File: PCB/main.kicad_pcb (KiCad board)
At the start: 2 copper layers, 112.9 x 63.7 mm, 126 parts, among them K1 HK19F-DCxxV-SHC, Q1 BC807, Q10 BC817, Q11 BC817, Q12 TPCA8120,L1Q, Q13 BC817, Q14 BC817, Q15 BC817, Q16 TPCA8120,L1Q, Q17 BC817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

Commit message: FET's Gate to NPN's collector resistor removed
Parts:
- removed RA15, RA16, RA17, RA18, RA19: 33K, Resistor_SMD:R_1206_3216Metric
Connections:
- Q12 pad 4: Net-(Q12-G) -> Net-(Q11-C)
- Q16 pad 4: Net-(Q16-G) -> Net-(Q13-C)
- Q7 pad 4: Net-(Q7-G) -> Net-(Q10-C)
- Q8 pad 3: Net-(Q8-C) -> Net-(Q5-G)
- Q9 pad 3: Net-(Q9-C) -> Net-(Q6-G)
- RA11 pad 2: Net-(Q7-G) -> Net-(Q10-C)
- RA12 pad 2: Net-(Q12-G) -> Net-(Q11-C)
- RA13 pad 2: Net-(Q16-G) -> Net-(Q13-C)
- RA3 pad 1: Net-(Q9-C) -> Net-(Q6-G)
- RA4 pad 1: Net-(Q8-C) -> Net-(Q5-G)
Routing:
- net Net-(Q11-C): track 30.2 -> 112.8 mm, vias 2 -> 4
- net Net-(Q12-G): track 81.4 -> 0.00 mm, vias 3 -> 0
- net Net-(Q13-C): track 61.2 -> 141.0 mm, vias 3 -> 8
- net Net-(Q16-G): track 76.9 -> 0.00 mm, vias 5 -> 0
- net Net-(Q5-G): track 64.2 -> 107.2 mm, vias 1 -> 3
- net Net-(Q8-C): track 40.1 -> 0.00 mm, vias 2 -> 0
- net Net-(Q10-C): track 79.0 -> 117.6 mm, vias 3 -> 4
- net Net-(Q7-G): track 35.6 -> 0.00 mm, vias 1 -> 0
- net +12V: track 268.3 -> 240.2 mm
- net Net-(Q6-G): track 129.5 -> 147.8 mm, vias 5 -> 6
- net Net-(Q9-C): track 18.3 -> 0.00 mm, vias 1 -> 0
- net ci_engineOFF: track 129.3 -> 126.4 mm
- net GND: track 501.9 -> 500.7 mm

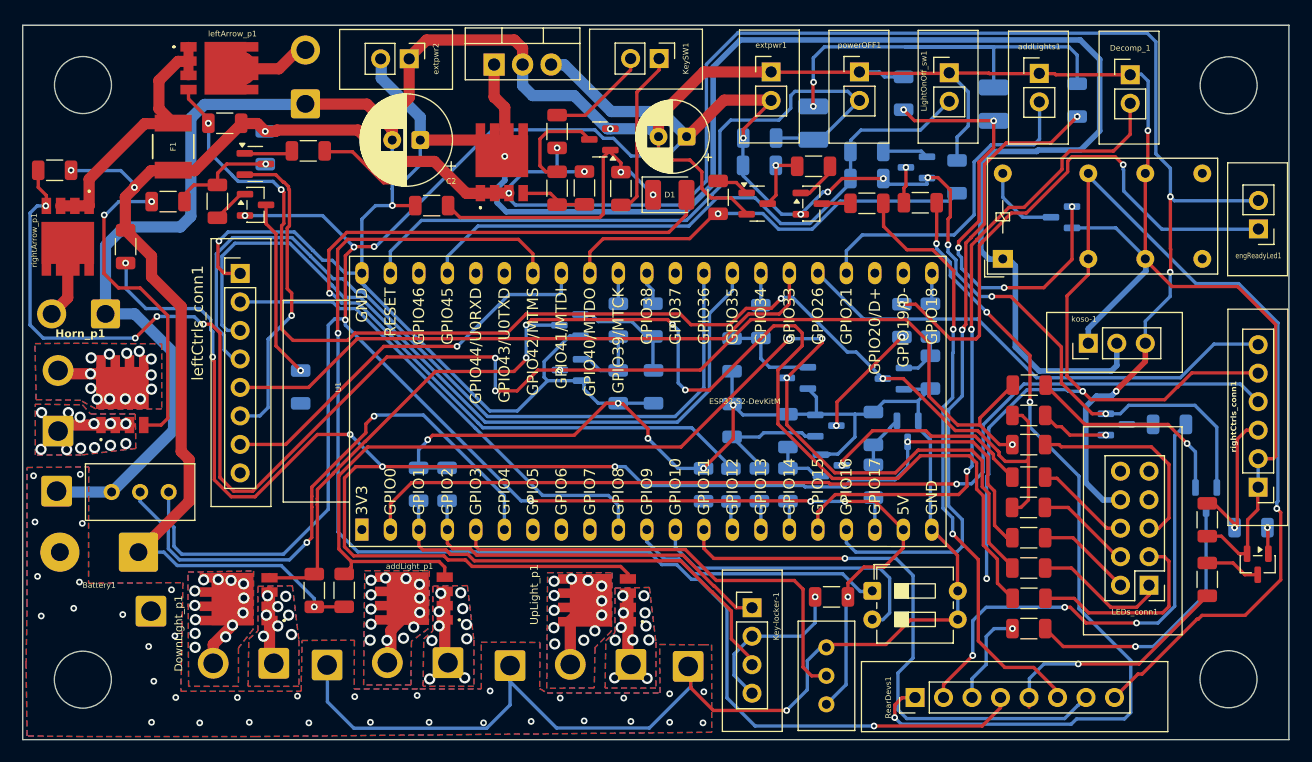
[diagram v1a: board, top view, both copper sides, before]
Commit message: Merge from ESP32__dualPCB branch
- DownLight: external fuse replaced by internal automatic one, wire connector replaced by 2.54 pin-header
- The resistor between FET's gate and NPN's collector has been removed
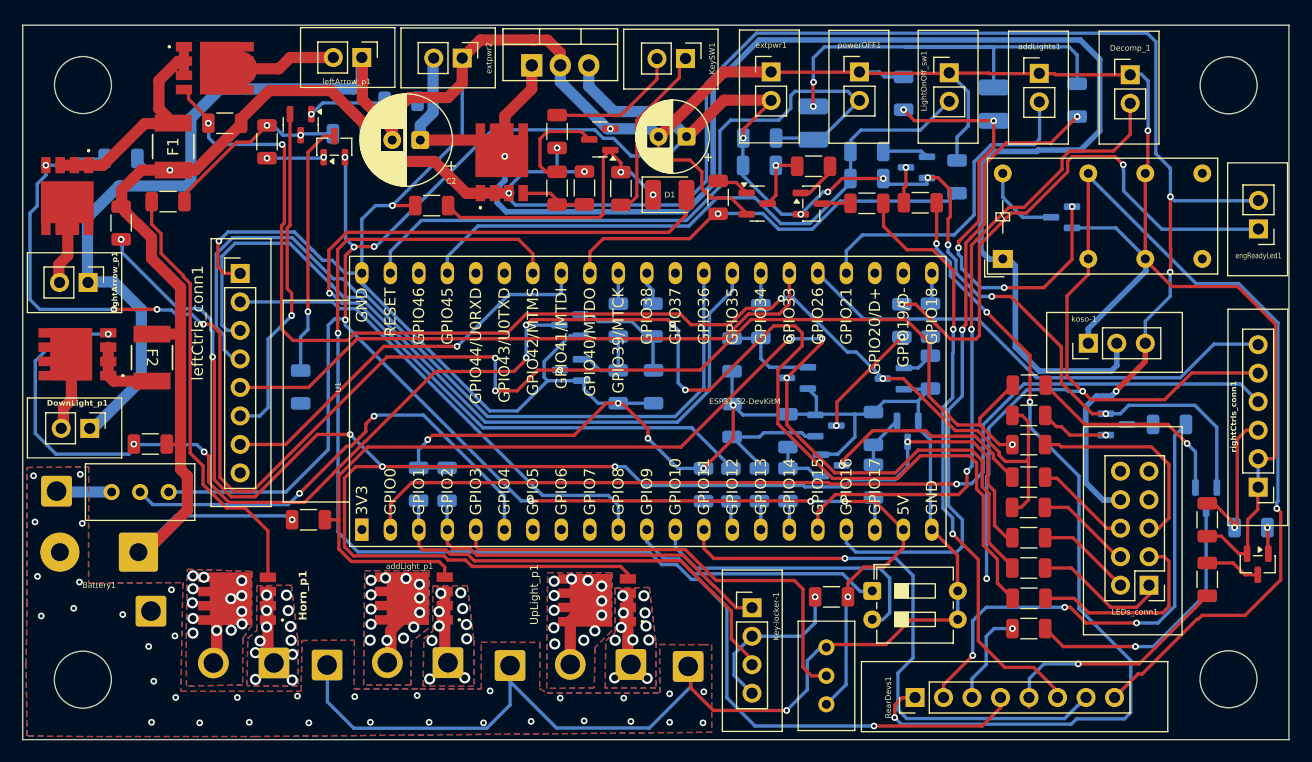
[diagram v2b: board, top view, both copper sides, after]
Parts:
- added F2: MF-MSMF050-2, MSMF:FUSE_F050-2, F.Cu at (65.8, 83.3)
- DownLight_p1: footprint Connector_Wire:SolderWire-1sqmm_1x02_P5.4mm_D1.4mm_OD2.7mm -> Connector_PinHeader_2.54mm:PinHeader_1x02_P2.54mm_Vertical
- F1: footprint MF-MSMF050-2:FUSE_F050-2 -> MSMF:FUSE_F050-2
- RA13, RA29: moved to B.Cu
- leftArrow_p1, rightArrow_p1: footprint Connector_Wire:SolderWire-0.75sqmm_1x02_P4.8mm_D1.25mm_OD2.3mm -> Connector_PinHeader_2.54mm:PinHeader_1x02_P2.54mm_Vertical
- moved Horn_p1 28.2 mm to (76.6, 110.6), turned to 180 degrees
- moved DownLight_p1 26.6 mm to (60.2, 89.7), turned to -90 degrees
- moved Q7 26.1 mm to (59.1, 83.0)
- moved Q18 20.9 mm to (73.3, 104.8), turned to 90 degrees
- moved RA11 19.6 mm to (65.6, 91.0), turned to 180 degrees
- moved RA29 9.38 mm to (88.0, 60.5)
- moved Q21 8.73 mm to (82.0, 64.5), turned to 90 degrees
- moved RA21 7.60 mm to (83.3, 63.4), turned to 0 degrees
- moved RA9 7.05 mm to (79.7, 97.8), turned to 0 degrees
- moved RA39 6.91 mm to (76.0, 64.1)
- moved leftArrow_p1 6.50 mm to (84.5, 56.6), turned to -90 degrees
- moved RA13 6.01 mm to (63.0, 65.6)
- moved Q17 5.35 mm to (79.0, 62.6), turned to -90 degrees
- moved extpwr2 4.73 mm to (93.4, 56.6)
- moved Q16 3.62 mm to (58.2, 69.0)
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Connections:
- DownLight_p1 pad 1: Net-(DownLight_p1-Pin_1) -> GND
- Q7 pad 1: Net-(DownLight_p1-Pin_1) -> Net-(Q7-S_1)
- Q7 pad 2: Net-(DownLight_p1-Pin_1) -> Net-(Q7-S_1)
- Q7 pad 3: Net-(DownLight_p1-Pin_1) -> Net-(Q7-S_1)
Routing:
- net Net-(Q10-C): track 117.6 -> 150.0 mm, vias 4 -> 7
- net 5V: track 267.7 -> 252.6 mm
- net tempPower: track 158.9 -> 145.7 mm, vias 2 -> 1
- net Net-(Q18-G): track 28.8 -> 38.8 mm, vias 2 -> 0
- net GND: track 500.7 -> 510.0 mm
- net Net-(U1-GPIO4/TOUCH4/ADC1_CH3): track 50.9 -> 42.6 mm
- net Net-(Q17-C): track 9.75 -> 16.8 mm, vias 1 -> 2
- net Net-(Q7-S_1): track 0.00 -> 6.64 mm
- net Net-(Q21-C): track 16.0 -> 22.7 mm
- net Net-(DownLight_p1-Pin_1): track 6.51 -> 0.00 mm, vias 8 -> 0
- net Net-(Q12-S_1): track 24.7 -> 21.4 mm
- net Net-(KeySW1-Pin_2): track 9.25 -> 12.1 mm
- net Net-(Q17-B): track 4.32 -> 7.01 mm, vias 0 -> 1
- net Net-(Q12-D_1): track 7.84 -> 10.5 mm
- net Net-(Q13-C): track 141.0 -> 143.3 mm
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- removed copper zone on B.Cu, net Net-(DownLight_p1-Pin_1)
- removed copper zone on F.Cu, net Net-(DownLight_p1-Pin_1)
- removed copper zone on B.Cu, net Net-(DownLight_p1-Pin_2)
- removed copper zone on F.Cu, net Net-(DownLight_p1-Pin_2)

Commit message: JST connectors for high current devices connectors
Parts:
- removed GND1, GND2: Conn_01x01, Connector_Wire:SolderWire-1sqmm_1x01_D1.4mm_OD2.7mm
- removed extpwr2: Conn_01x02, Connector_PinHeader_2.54mm:PinHeader_1x02_P2.54mm_Vertical
- added Horn_p2: Conn_01x01, Connector_Wire:SolderWire-1sqmm_1x01_D1.4mm_OD2.7mm, F.Cu at (75.2, 105.8)
- added UpLight_p2: Conn_01x01, Connector_Wire:SolderWire-1sqmm_1x01_D1.4mm_OD2.7mm, F.Cu at (103.0, 105.8)
- added addLight_p2: Conn_01x01, Connector_Wire:SolderWire-1sqmm_1x01_D1.4mm_OD2.7mm, F.Cu at (88.5, 105.8)
- added rearDevsPwr1: Conn_01x02, Connector_PinHeader_2.54mm:PinHeader_1x02_P2.54mm_Vertical, F.Cu at (93.3, 56.6)
- Horn_p1, UpLight_p1, addLight_p1: footprint Connector_Wire:SolderWire-1sqmm_1x02_P5.4mm_D1.4mm_OD2.7mm -> Connector_JST:JST_VH_B2P-VH_1x02_P3.96mm_Vertical
- Q18, Q5, Q6: moved to B.Cu
- moved Q18 7.98 mm to (81.3, 105.2)
- moved GND3 7.57 mm to (74.0, 112.5)
- moved GND5 7.36 mm to (68.8, 112.6)
- moved Q5 5.72 mm to (94.8, 105.2)
- moved Q6 3.69 mm to (109.1, 105.1)
- moved Horn_p1 3.05 mm to (79.3, 112.0), turned to 0 degrees
- moved UpLight_p1 1.88 mm to (107.2, 112.1), turned to 0 degrees
- moved addLight_p1 1.70 mm to (92.9, 112.0), turned to 0 degrees
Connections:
- Horn_p1 pad 1: Net-(Horn_p1-Pin_1) -> GND
- Q18 pad 1: Net-(Horn_p1-Pin_1) -> Net-(Horn_p2-Pin_1)
- Q18 pad 2: Net-(Horn_p1-Pin_1) -> Net-(Horn_p2-Pin_1)
- Q18 pad 3: Net-(Horn_p1-Pin_1) -> Net-(Horn_p2-Pin_1)
- UpLight_p1 pad 1: Net-(Q6-S_1) -> GND
- addLight_p1 pad 1: Net-(Q5-S_1) -> GND
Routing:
- net GND: track 510.0 -> 468.4 mm, vias 45 -> 26
- net Net-(Horn_p1-Pin_2): track 7.00 -> 0.00 mm, vias 13 -> 8
- net Net-(Horn_p1-Pin_1): track 6.74 -> 0.00 mm, vias 12 -> 0
- net Net-(Q6-D_1): track 6.47 -> 0.00 mm, vias 12 -> 9
- net Net-(Q6-S_1): track 6.46 -> 3.41 mm, vias 11 -> 7
- net Net-(Q6-G): track 148.4 -> 146.4 mm, vias 6 -> 7
- net Net-(Q18-G): track 38.8 -> 40.1 mm, vias 0 -> 1
- net Net-(Q5-D_1): track 6.47 -> 5.32 mm, vias 13 -> 9
- net Net-(Q5-G): track 107.1 -> 107.6 mm, vias 3 -> 4
- net Net-(Q5-S_1): track 6.47 -> 6.05 mm, vias 10 -> 7
- net Net-(Horn_p2-Pin_1): vias 0 -> 7
- added copper zone on B.Cu, net Net-(Horn_p2-Pin_1)
- added copper zone on F.Cu, net Net-(Horn_p2-Pin_1)
- removed copper zone on B.Cu, net Net-(Horn_p1-Pin_1)
- removed copper zone on F.Cu, net Net-(Horn_p1-Pin_1)

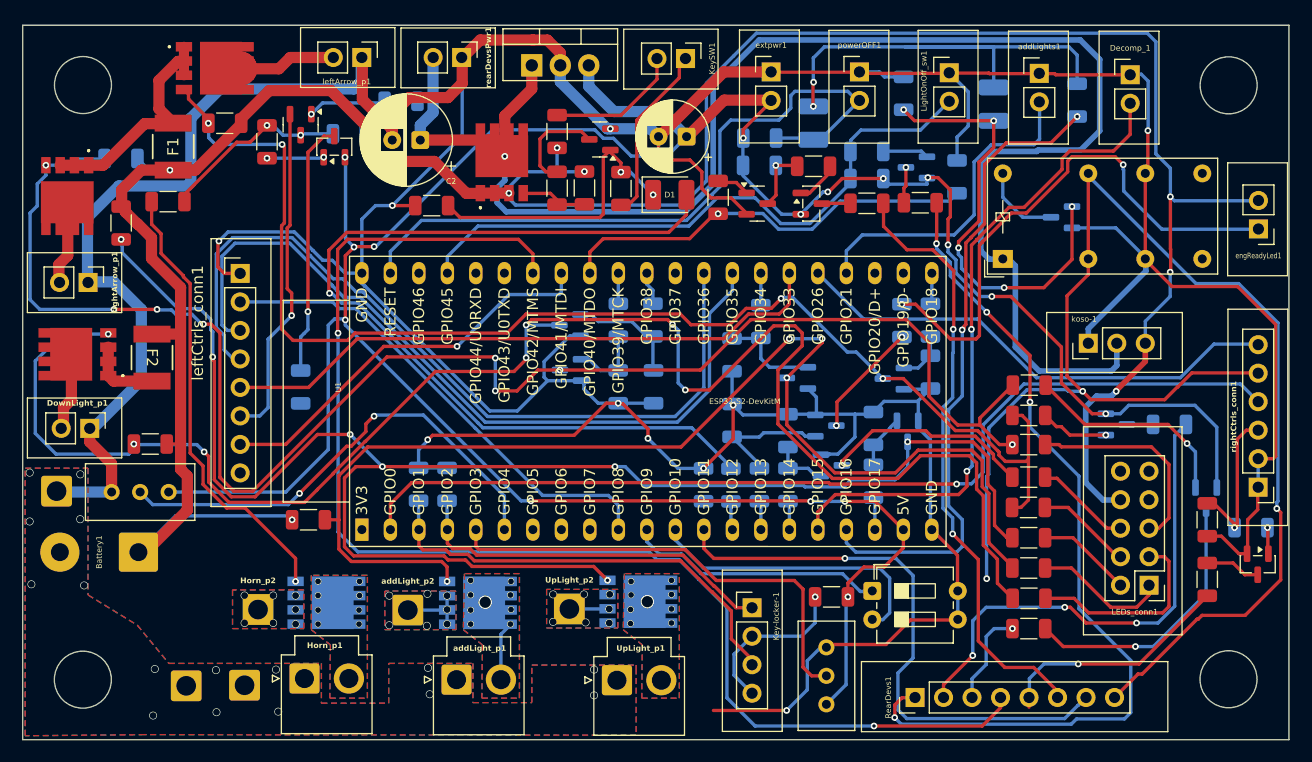
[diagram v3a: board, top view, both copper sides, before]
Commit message: JST connector orientation fixed (female for PCB)
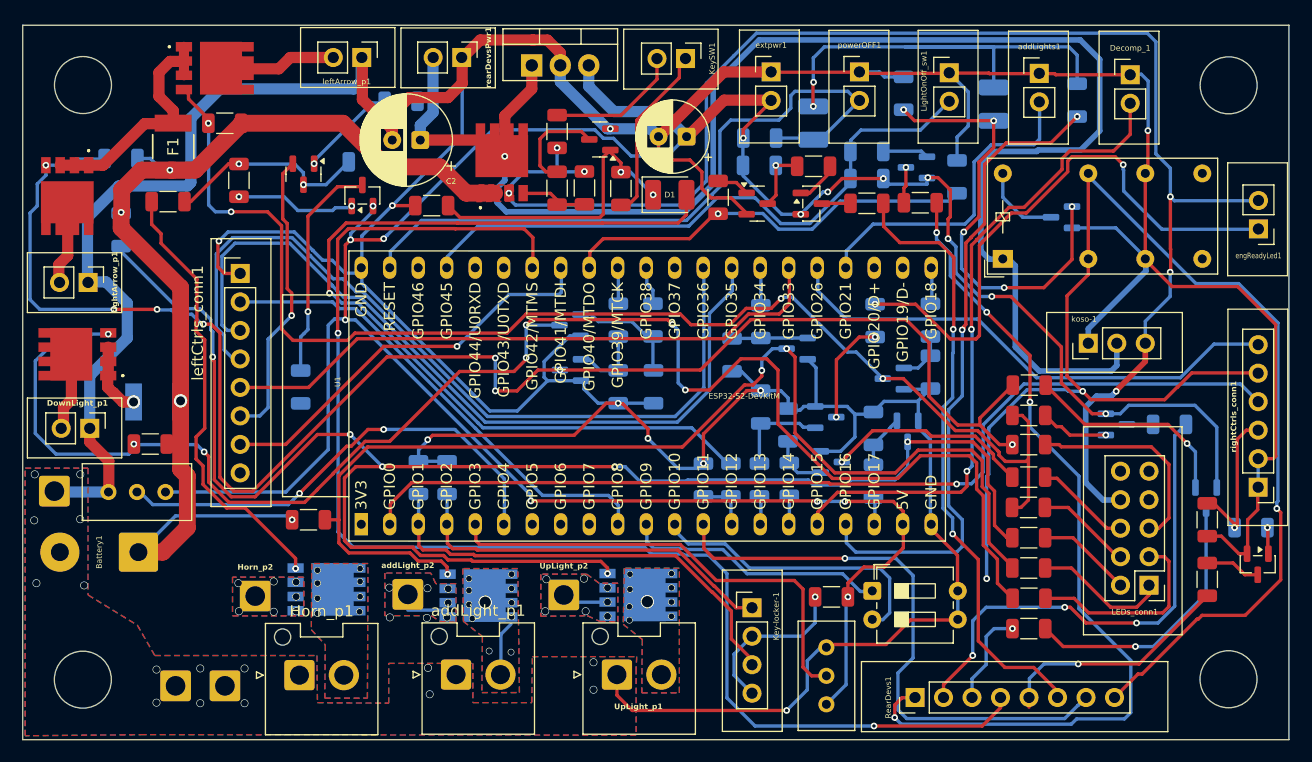
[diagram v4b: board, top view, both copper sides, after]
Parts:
- F2, RA10: moved to B.Cu
- Horn_p1, UpLight_p1, addLight_p1: footprint Connector_JST:JST_VH_B2P-VH_1x02_P3.96mm_Vertical -> Connector_JST:JST_VH_B2P-VH-FB-B_1x02_P3.96mm_Vertical
- moved Q21 5.02 mm to (84.5, 68.9)
- moved Q17 4.42 mm to (79.2, 67.0)
- moved RA39 4.25 mm to (73.5, 67.5)
- moved F2 3.98 mm to (66.2, 87.3), turned to 180 degrees
- moved RA21 2.87 mm to (84.8, 65.9)
- moved RA28 2.82 mm to (120.0, 87.8)
- moved Q8 2.61 mm to (123.2, 82.5)
- moved RA14 2.39 mm to (130.2, 80.0)
- moved GND3 1.75 mm to (72.2, 112.6)
- moved addLight_p2 1.40 mm to (88.5, 104.5)
- moved UpLight_p2 1.35 mm to (102.5, 104.5)
- moved Horn_p2 1.23 mm to (75.0, 104.6)
- moved Q18 1.19 mm to (81.3, 104.0)
- moved GND5 0.95 mm to (67.8, 112.6)
- moved Q15 0.76 mm to (125.8, 88.7)
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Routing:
- net GND: track 468.4 -> 479.7 mm
- net Net-(Q10-C): track 150.0 -> 142.5 mm
- net +12V: track 238.9 -> 232.1 mm, vias 9 -> 11
- net Net-(Q5-G): track 107.6 -> 101.8 mm, vias 4 -> 3
- net Net-(Q21-B): track 5.09 -> 10.7 mm
- net ci_horn: track 30.1 -> 26.1 mm
- net i_bykeStand: track 117.7 -> 121.2 mm
- net Net-(Q15-B): track 11.5 -> 8.71 mm
- net Net-(Q21-C): track 22.7 -> 20.0 mm
- net 5V: track 252.6 -> 250.1 mm
- net Net-(Q5-S_1): track 6.05 -> 3.58 mm
- net Net-(engReadyLed1-Pin_1): track 49.3 -> 51.7 mm
- net Net-(Q8-B): track 8.93 -> 6.75 mm
- net Net-(Q12-D_1): track 10.5 -> 8.69 mm
- net Net-(Q17-B): track 7.01 -> 8.75 mm
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- added copper zone on F.Cu, net +12V

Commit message: Also the power connector is a JST one!
Except for the external fuses, the PCB has NO one welded wire!
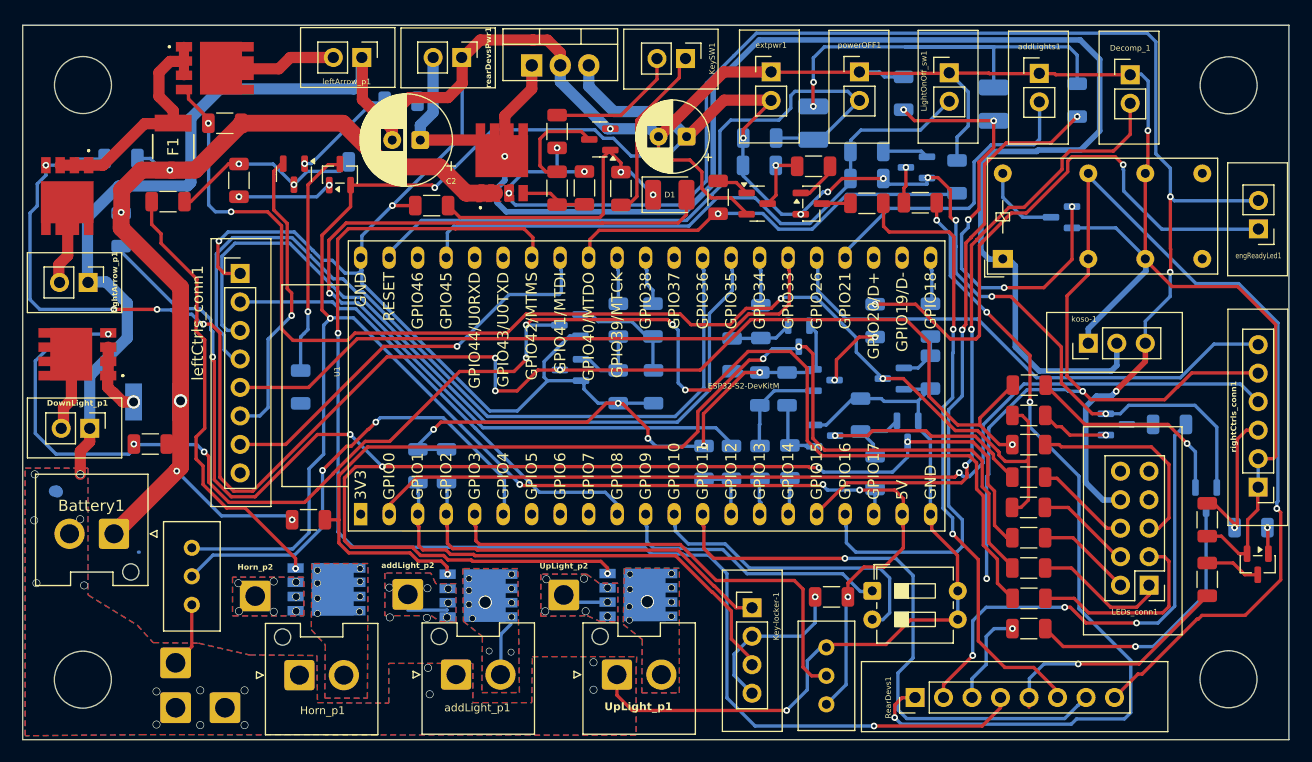
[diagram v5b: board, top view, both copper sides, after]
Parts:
- Battery1: footprint Connector_Wire:SolderWire-0.75sqmm_1x02_P7mm_D1.25mm_OD3.5mm -> Connector_JST:JST_VH_B2P-VH-FB-B_1x02_P3.96mm_Vertical
- moved GND4 18.7 mm to (67.8, 110.5)
- moved RV2 5.50 mm to (69.3, 100.3), turned to 90 degrees
- moved Q15 3.30 mm to (125.7, 85.3)
- moved RA27 3.21 mm to (122.3, 86.1)
- moved Q21 2.73 mm to (82.5, 67.0)
- moved Battery1 2.72 mm to (62.4, 99.0)
- moved Q14 2.43 mm to (125.7, 90.3)
- moved GND3 1.95 mm to (72.2, 114.5)
- moved GND5 1.95 mm to (67.8, 114.5)
- moved RA22 1.66 mm to (128.9, 88.5)
- moved RA28 1.61 mm to (119.9, 86.1)
- moved R11 1.56 mm to (117.4, 92.7)
- moved R12 1.56 mm to (115.0, 92.7)
- moved RA30 1.56 mm to (119.9, 92.7)
- moved RA31 1.56 mm to (122.6, 92.6)
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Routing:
- net GND: track 479.7 -> 470.5 mm
- net +12V: track 232.1 -> 226.5 mm, vias 11 -> 12
- net 5V: track 250.1 -> 254.3 mm, vias 16 -> 14
- net Net-(Q15-C): track 9.40 -> 6.16 mm
- net Net-(Q21-B): track 10.7 -> 8.48 mm
- net Net-(Q9-B): track 4.79 -> 6.45 mm
- net Net-(Q6-G): track 145.5 -> 143.9 mm
- net i_addLight: track 29.0 -> 27.5 mm
- net Net-(Q8-B): track 6.75 -> 5.47 mm
- net i_decompr: track 58.6 -> 57.4 mm
- net i_startButton: track 86.8 -> 85.7 mm
- net i_Vx1: track 40.5 -> 41.6 mm
- net i_Vx2: track 34.0 -> 35.1 mm
- net co_startEngine: track 55.6 -> 56.6 mm
- net Net-(Q15-B): track 8.71 -> 9.72 mm
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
